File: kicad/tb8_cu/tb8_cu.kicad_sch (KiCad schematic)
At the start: 45 parts, among them J1 Conn_02x25_Counter_Clockwise, U1 74AHCT74, U10 74AHCT193, U11 74AHCT193, U12 74AHCT193, U13 74AHCT193, U14 74AHCT573, U15 74AHCT573, U16 74HC00, U17 74HC00, U18 74HCT74, U19 74AHCT573, U2 74AHCT08, U20 74AHCT573, U21 74AHCT573, U22 74AHCT573, U3 74AHCT32, U4 74AHCT573, U5 74AHCT238, U6 74AHCT238, U7 74AHCT573, U8 74AHCT00, U9 74AHCT573

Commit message: EBC25DCWN footprint
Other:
- company: (none) -> Dante Morelli
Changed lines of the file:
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@@
 	(title_block
 		(title "tb8 Control Unit Card")
-		(date "2025-11-28")
+		(date "2025-11-29")
 		(rev "0.1")
+		(company "Dante Morelli")
 	)
 	(text "Unused Logic"

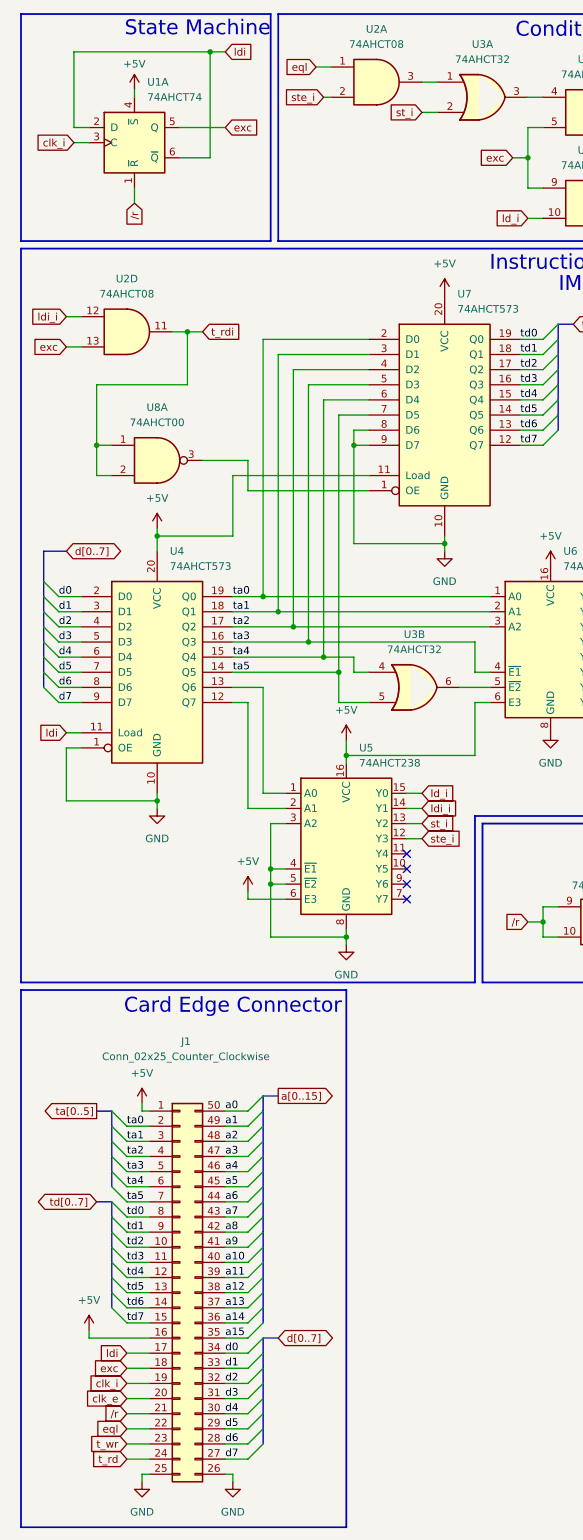
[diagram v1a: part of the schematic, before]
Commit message: Rename labels ste->stc and eql->cmp
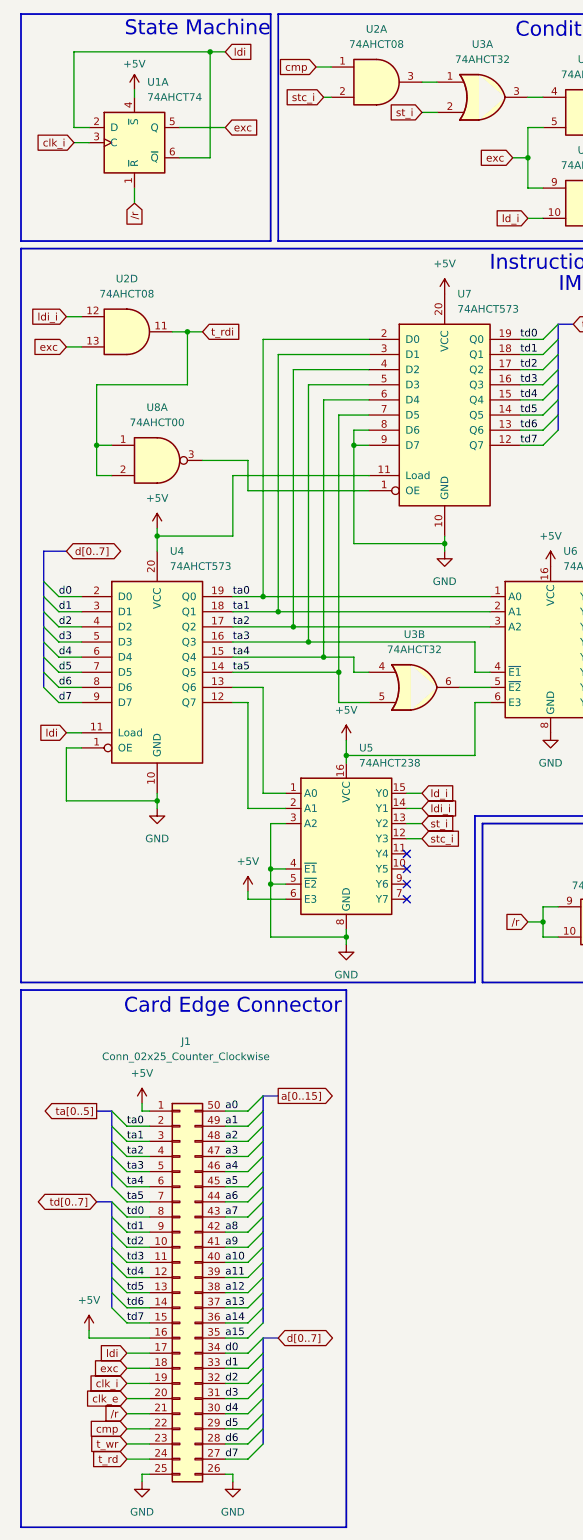
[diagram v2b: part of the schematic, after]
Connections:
- net eql renamed cmp
- net ste_i renamed stc_i
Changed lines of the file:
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@@
 		)
 	)
-	(global_label "eql"
+	(global_label "cmp"
 		(shape input)
 		(at 30.48 250.19 180)
@@
 		)
 		(property "Intersheetrefs" "${INTERSHEET_REFS}"
-			(at 24.592 250.19 0)
+			(at 23.5639 250.19 0)
 			(effects
 				(font
@@
 		)
 	)
-	(global_label "ste_i"
+	(global_label "stc_i"
 		(shape input)
 		(at 63.5 26.67 180)
@@
 		)
 	)
-	(global_label "ste_i"
+	(global_label "stc_i"
 		(shape input)
 		(at 80.01 151.13 0)
@@
 		)
 	)
-	(global_label "eql"
+	(global_label "cmp"
 		(shape input)
 		(at 62.23 21.59 180)
@@
 		)
 		(property "Intersheetrefs" "${INTERSHEET_REFS}"
-			(at 56.342 21.59 0)
-			(effects
-				(font
+			(at 55.3139 21.59 0)
+			(effects
+				(font

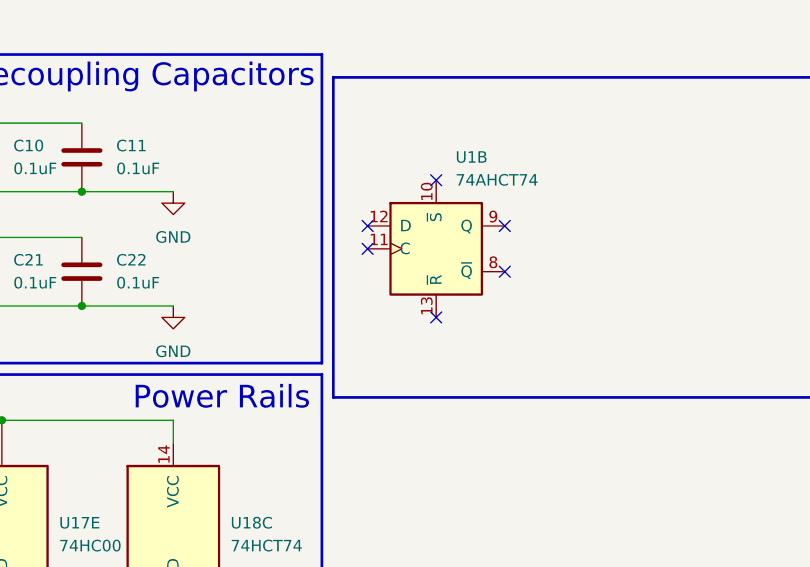
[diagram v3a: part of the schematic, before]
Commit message: ground unused flipflop inputs
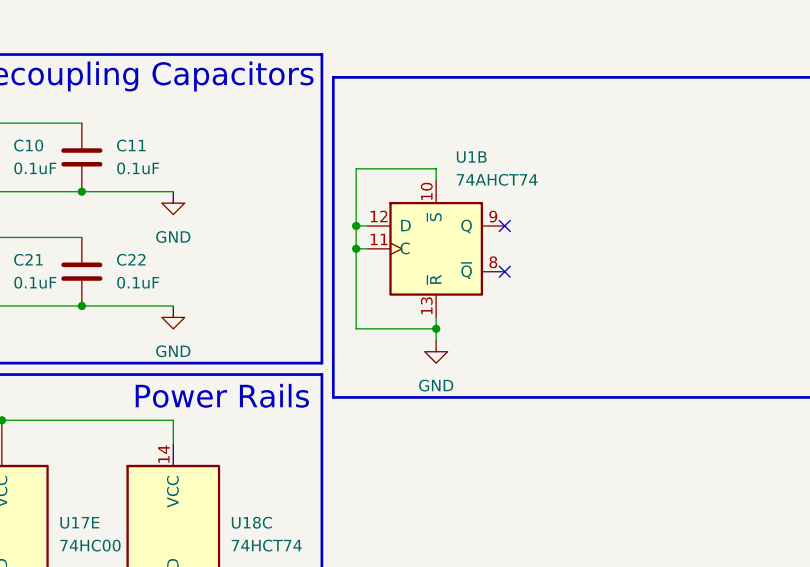
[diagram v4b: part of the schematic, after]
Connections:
- net GND: now also U1.10 (~{S}), U1.11 (C), U1.12 (D), U1.13 (~{R})
- no-connect marks 20 -> 16
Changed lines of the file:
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@@
 	)
 	(junction
+		(at 314.96 217.17)
+		(diameter 0)
+		(color 0 0 0 0)
+	)
+	(junction
 		(at 140.97 151.13)
 		(diameter 0)
@@
 	)
 	(junction
+		(at 314.96 214.63)
+		(diameter 0)
+		(color 0 0 0 0)
+	)
+	(junction
 		(at 55.88 113.03)
 		(diameter 0)
@@
 	)
 	(junction
+		(at 323.85 226.06)
+		(diameter 0)
+		(color 0 0 0 0)
+	)
+	(junction
 		(at 184.15 151.13)
 		(diameter 0)
@@
 	)
 	(no_connect
-		(at 316.23 217.17)
-	)
-	(no_connect
-		(at 323.85 224.79)
-	)
-	(no_connect
 		(at 111.76 120.65)
 	)
@@
 	)
 	(no_connect
-		(at 316.23 214.63)
-	)
-	(no_connect
 		(at 331.47 219.71)
 	)
@@
 	)
 	(no_connect
-		(at 323.85 209.55)
-	)
-	(no_connect
 		(at 111.76 118.11)
 	)
@@
 		)
 	)
+	(wire
+		(pts
+			(xy 316.23 217.17) (xy 314.96 217.17)
+		)
+		(stroke
+			(width 0)
+			(type default)
+		)
+	)
 	(bus
 		(pts
@@
 		)
 	)
+	(wire
+		(pts
+			(xy 323.85 226.06) (xy 323.85 227.33)
+		)
+		(stroke
+			(width 0)
+			(type default)
+		)
+	)
 	(bus
 		(pts
@@
 		)
 	)
+	(wire
+		(pts
+			(xy 323.85 208.28) (xy 314.96 208.28)
+		)
+		(stroke
+			(width 0)
+			(type default)
+		)
+	)
 	(bus
 		(pts
@@
 		)
 	)
+	(wire
+		(pts
+			(xy 314.96 217.17) (xy 314.96 226.06)
+		)
+		(stroke
+			(width 0)
+			(type default)
+		)
+	)
 	(bus
 		(pts
@@
 	(wire
 		(pts
+			(xy 314.96 214.63) (xy 314.96 217.17)
+		)
+		(stroke
+			(width 0)
+			(type default)
+		)
+	)
+	(wire
+		(pts
 			(xy 177.8 102.87) (xy 181.61 102.87)
 		)
@@
 		)
 	)
+	(wire
+		(pts
+			(xy 323.85 209.55) (xy 323.85 208.28)
+		)
+		(stroke
+			(width 0)
+			(type default)
+		)
+	)
 	(bus
 		(pts
@@
 	(wire
 		(pts
+			(xy 314.96 208.28) (xy 314.96 214.63)
+		)
+		(stroke
+			(width 0)
+			(type default)
+		)
+	)
+	(wire
+		(pts
 			(xy 194.31 179.07) (xy 151.13 179.07)
 		)
@@
 	(wire
 		(pts
+			(xy 316.23 214.63) (xy 314.96 214.63)
+		)
+		(stroke
+			(width 0)
+			(type default)
+		)
+	)
+	(wire
+		(pts
 			(xy 252.73 53.34) (xy 264.16 53.34)
 		)
@@
 	(wire
 		(pts
+			(xy 314.96 226.06) (xy 323.85 226.06)
+		)
+		(stroke
+			(width 0)
+			(type default)
+		)
+	)
+	(wire
+		(pts
 			(xy 30.48 222.25) (xy 34.29 222.25)
 		)
@@
 	(wire
 		(pts
+			(xy 323.85 224.79) (xy 323.85 226.06)
+		)
+		(stroke
+			(width 0)
+			(type default)
+		)
+	)
+	(wire
+		(pts
 			(xy 222.25 215.9) (xy 232.41 215.9)
 		)
@@
 				)
 			)
+		)
+	)
+	(symbol
+		(lib_id "power:GND")
+		(at 323.85 227.33 0)
+		(unit 1)
+		(exclude_from_sim no)
+		(in_bom yes)
+		(on_board yes)
+		(dnp no)
+		(fields_autoplaced yes)
+		(property "Reference" "#PWR050"
+			(at 323.85 233.68 0)
+			(effects
+				(font
+					(size 1.27 1.27)
+				)
+				(hide yes)
+			)
+		)
+		(property "Value" "GND"
+			(at 323.85 232.41 0)
+			(effects
+				(font
+					(size 1.27 1.27)
+				)
+			)
+		)
+		(property "Footprint" ""
+			(at 323.85 227.33 0)
+			(effects
+				(font
+					(size 1.27 1.27)
+				)
+				(hide yes)
+			)
+		)
+		(property "Datasheet" ""
+			(at 323.85 227.33 0)
+			(effects
+				(font
+					(size 1.27 1.27)
+				)
+				(hide yes)
+			)
+		)
+		(property "Description" "Power symbol creates a global label with name \"GND\" , ground"
+			(at 323.85 227.33 0)
+			(effects
+				(font
+					(size 1.27 1.27)
+				)
+				(hide yes)
+			)
+		)
+		(pin "1"
+		)
+		(instances
+			(project ""
+				(path "/d66ecd5d-5c45-4e8a-8529-bc552f1a1fa5"
+					(reference "#PWR050")
+					(unit 1)
+				)
+			)

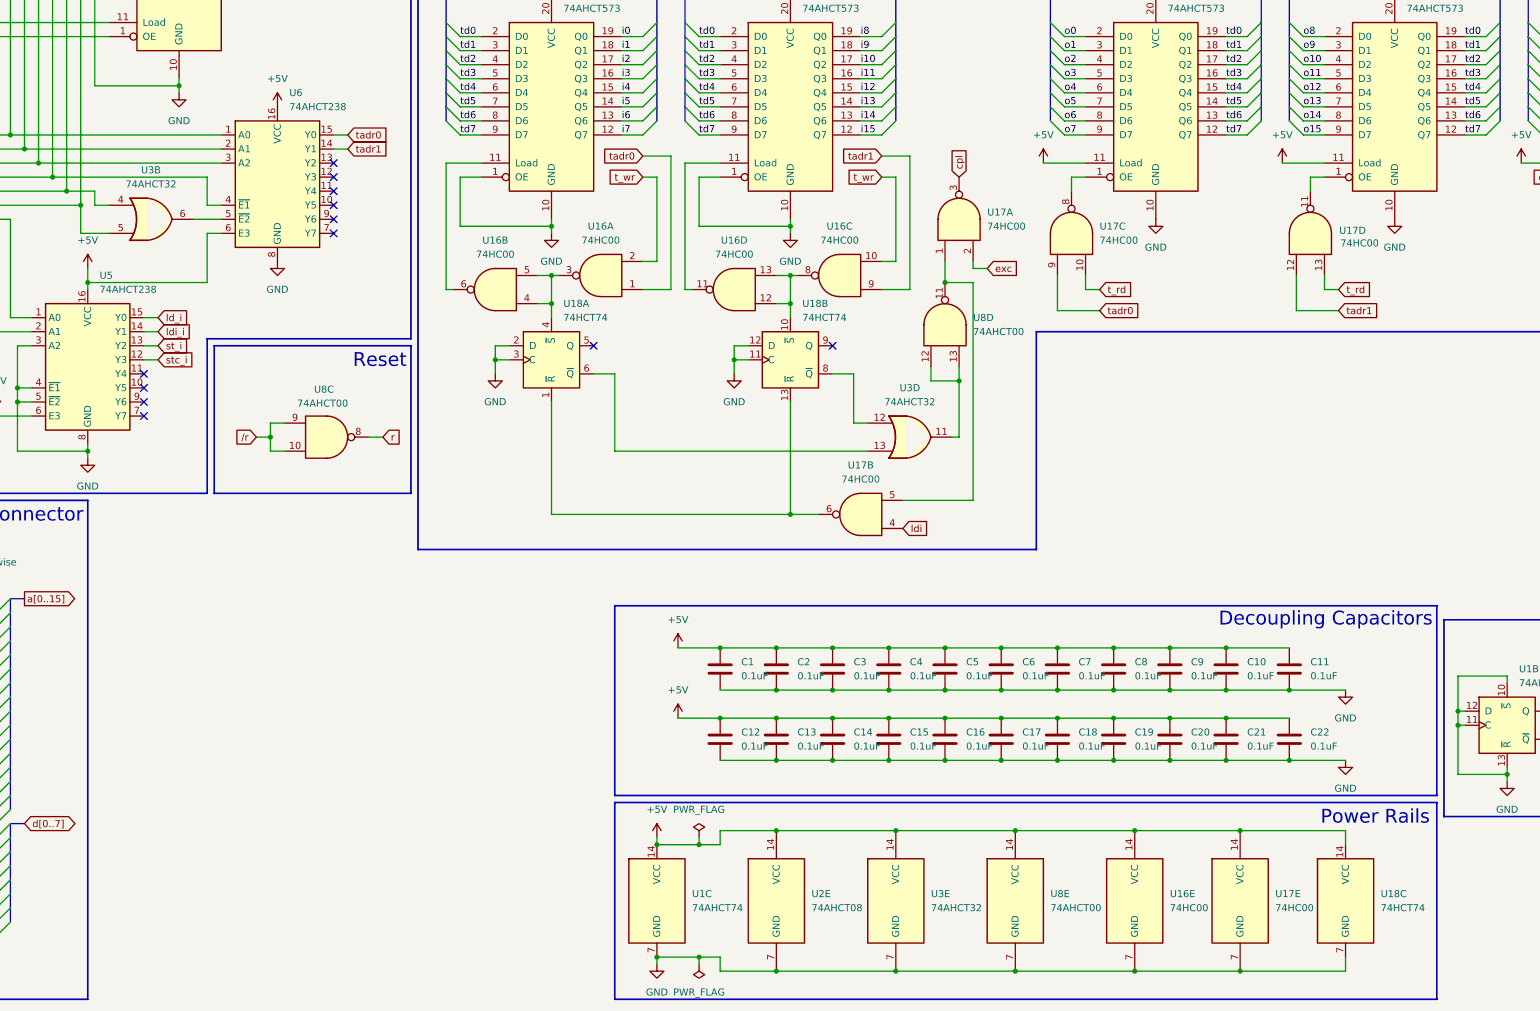
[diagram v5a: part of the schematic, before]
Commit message: fix/rotate pcb labels
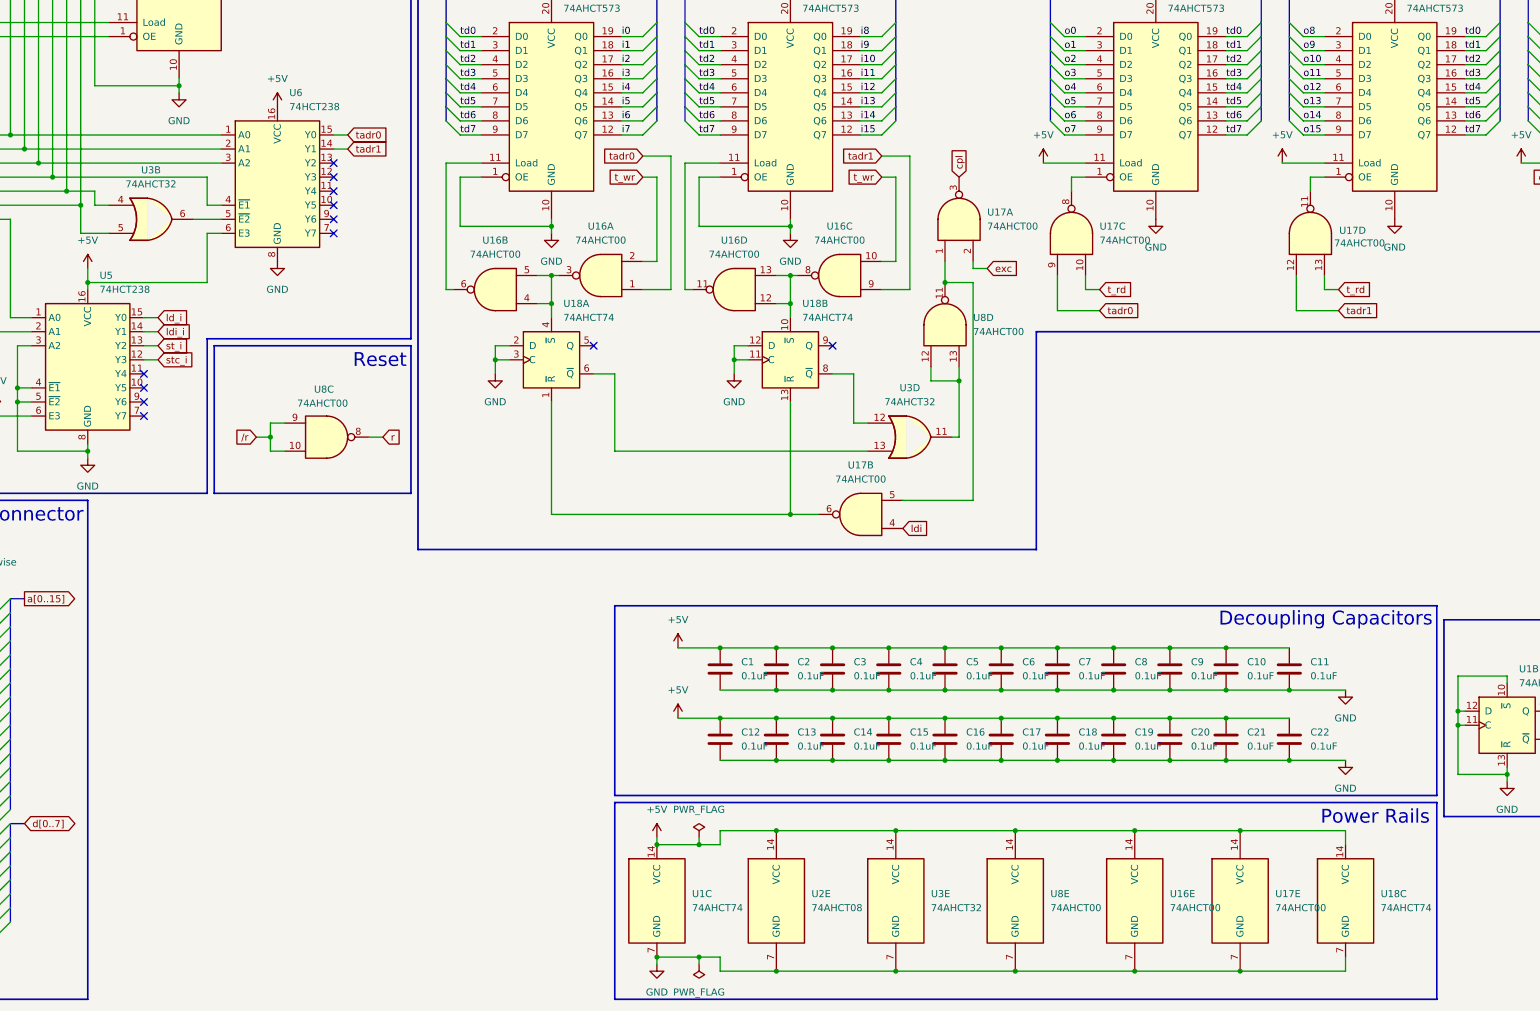
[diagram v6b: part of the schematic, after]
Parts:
- U16, U17: value 74HC00 -> 74AHCT00
- U18: value 74HCT74 -> 74AHCT74
- U5, U6: value 74AHCT238 -> 74HCT238
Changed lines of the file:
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@@
 	(title_block
 		(title "tb8 Control Unit Card")
-		(date "2025-12-16")
+		(date "2026-01-08")
 		(rev "1.0")
 		(company "Dante Morelli")
@@
 			)
 		)
-		(property "Value" "74HC00"
+		(property "Value" "74AHCT00"
 			(at 140.9783 132.08 0)
 			(effects
@@
 			)
 		)
-		(property "Value" "74HCT74"
+		(property "Value" "74AHCT74"
 			(at 153.2733 143.51 0)
 			(effects
@@
 			)
 		)
-		(property "Value" "74HC00"
+		(property "Value" "74AHCT00"
 			(at 297.18 130.048 90)
 			(effects
@@
 			)
 		)
-		(property "Value" "74AHCT238"
+		(property "Value" "74HCT238"
 			(at 69.4533 138.43 0)
 			(effects
@@
 			)
 		)
-		(property "Value" "74HC00"
+		(property "Value" "74AHCT00"
 			(at 281.94 250.1899 0)
 			(effects
@@
 			)
 		)
-		(property "Value" "74HCT74"
+		(property "Value" "74AHCT74"
 			(at 300.99 250.1899 0)
 			(effects
@@
 			)
 		)
-		(property "Value" "74HC00"
+		(property "Value" "74AHCT00"
 			(at 207.0183 172.72 0)
 			(effects
@@
 			)
 		)
-		(property "Value" "74HC00"
+		(property "Value" "74AHCT00"
 			(at 203.2083 129.54 0)
 			(effects
@@
 			)
 		)
-		(property "Value" "74HC00"
+		(property "Value" "74AHCT00"
 			(at 250.19 129.5482 90)
 			(effects
@@
 			)
 		)
-		(property "Value" "74HC00"
+		(property "Value" "74AHCT00"
 			(at 160.0283 129.54 0)
 			(effects
@@
 			)
 		)
-		(property "Value" "74AHCT238"
+		(property "Value" "74HCT238"
 			(at 103.7433 105.41 0)
 			(effects
@@
 			)
 		)
-		(property "Value" "74HC00"
+		(property "Value" "74AHCT00"
 			(at 262.89 250.1899 0)
 			(effects
@@
 			)
 		)
-		(property "Value" "74HCT74"
+		(property "Value" "74AHCT74"
 			(at 196.4533 143.51 0)
 			(effects
@@
 			)
 		)
-		(property "Value" "74HC00"
+		(property "Value" "74AHCT00"
 			(at 184.1583 132.08 0)
 			(effects
@@
 			)
 		)
-		(property "Value" "74HC00"
+		(property "Value" "74AHCT00"
 			(at 229.87 127.0082 90)
 			(effects
